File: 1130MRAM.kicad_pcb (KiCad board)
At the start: 4 copper layers, 228.6 x 63.5 mm, 159 parts, among them IC1 BSV52LT1G, IC10 BSV52LT1G, IC11 BSV52LT1G, IC12 BSV52LT1G, IC13 BSV52LT1G, IC14 BSV52LT1G, IC15 BSV52LT1G, IC16 BSV52LT1G, IC17 BSV52LT1G, IC18 BSV52LT1G, IC2 BSV52LT1G, IC3 BSV52LT1G, IC4 BSV52LT1G, IC5 BSV52LT1G, IC6 BSV52LT1G, IC7 BSV52LT1G, IC8 BSV52LT1G, IC9 BSV52LT1G, J1 Screw_Terminal_01x03, J1A09 SLTpad, J1A11 SLTpad, J2 Screw_Terminal_01x03, K1E09 SLTpad, K1E11 SLTpad, M1A09 SLTpad, M1A11 SLTpad, M1C09 SLTpad, M1D09 SLTpad, M1E09 SLTpad, M1E11 SLTpad, SW1 SLTpad, U1 MR0A16AYS35, U10 74LVC08A, U11 74LVC08A, U12 SN74LVC1G123DCUR, U13 SN74LVC1G123DCUR, U14 74HC00, U15 74HC86, U16 74HC86, U17 74HC86, U18 74HC86, U2 SN74LV240APWR, U3 SN74LV240APWR, U4 LDL1117, U5 SN74LVC1G123DCUR, U6 SN74LVC1G123DCUR, U7 74LVC08A, U8 74LVC08A, U9 74LVC08A

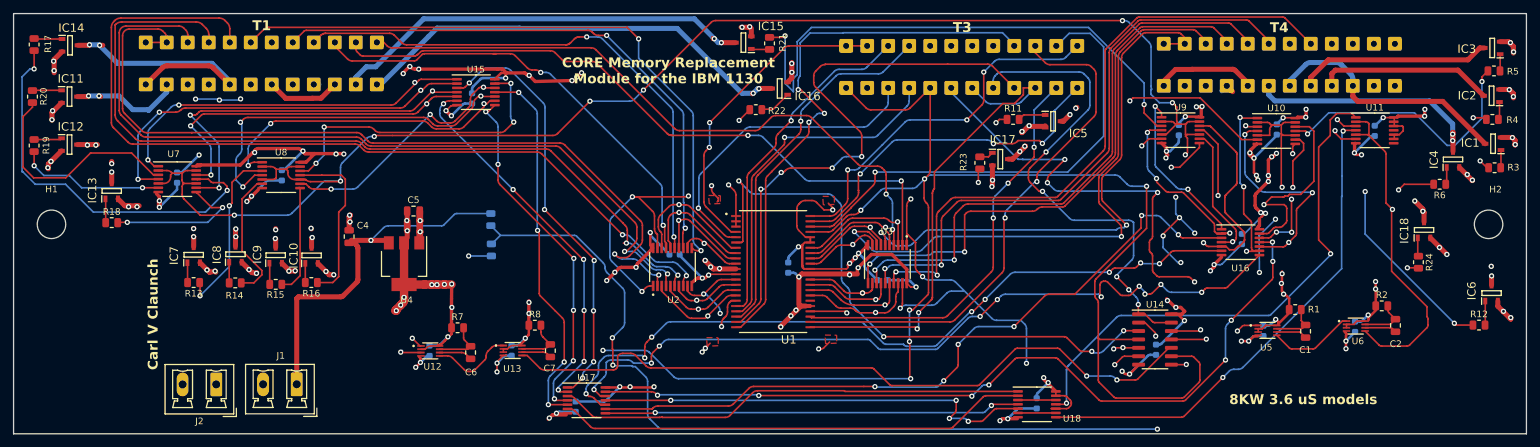
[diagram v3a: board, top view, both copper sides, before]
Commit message: New version leveraging FPGA
Changed board to be driven by an FPGA
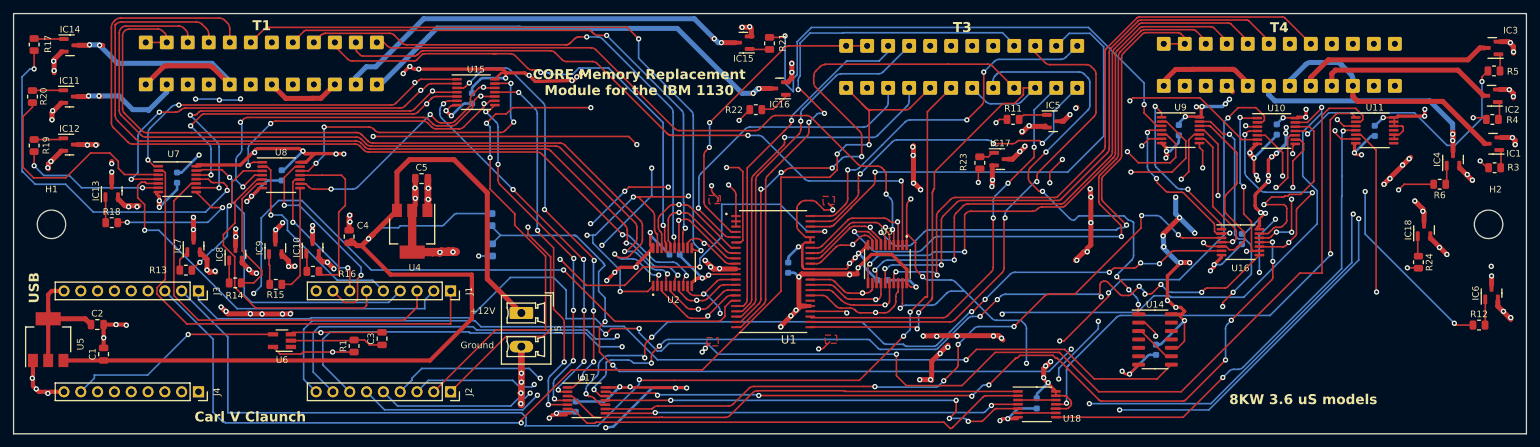
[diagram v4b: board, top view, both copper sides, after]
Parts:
- removed C14, C15, C22, C23: 0.1uF, Capacitor_SMD:C_0603_1608Metric
- removed C6: 680pF, Capacitor_SMD:C_0805_2012Metric
- removed C7: 47pF, Capacitor_SMD:C_0805_2012Metric
- removed R2, R7, R8: 1K, Resistor_SMD:R_0805_2012Metric
- removed U12, U13: SN74LVC1G123DCUR, 1130MRAM:sn74lvc1g123dcur
- added C3: 4.7u, Capacitor_SMD:C_0805_2012Metric, F.Cu at (88.7, 105.0)
- added J3: Conn_01x09_MountingPin, Connector_PinSocket_2.54mm:PinSocket_1x09_P2.54mm_Vertical, F.Cu at (61.0, 97.8)
- added J4: Conn_01x09_MountingPin, Connector_PinSocket_2.54mm:PinSocket_1x09_P2.54mm_Vertical, F.Cu at (61.0, 113.0)
- added J5: Screw_Terminal_01x03, Connector_Phoenix_MC_HighVoltage:PhoenixContact_MCV_1,5_2-G-5.08_1x02_P5.08mm_Vertical, F.Cu at (109.8, 101.1)
- C1: value 680pF -> 1uF
- C2: value 33pF -> 4.7uF
- IC1, IC10, IC11, IC12, IC13, IC14, IC15, IC16, IC17, IC18, IC2, IC3, IC4, IC5, IC6, IC7, IC8, IC9: footprint SamacSys_Parts:SOT95P237X111-3N -> Package_TO_SOT_SMD:SOT-23
- J1, J2: value Screw_Terminal_01x03 -> Conn_01x09_MountingPin; footprint Connector_Phoenix_MC_HighVoltage:PhoenixContact_MCV_1,5_2-G-5.08_1x02_P5.08mm_Vertical -> Connector_PinSocket_2.54mm:PinSocket_1x09_P2.54mm_Vertical
- R1: value 1K -> 330k
- U5: value SN74LVC1G123DCUR -> LDL1117; footprint 1130MRAM:sn74lvc1g123dcur -> Package_TO_SOT_SMD:SOT-223-3_TabPin2
- U6: value SN74LVC1G123DCUR -> 74LVC1G14; footprint 1130MRAM:sn74lvc1g123dcur -> Package_TO_SOT_SMD:SOT-23-5_HandSoldering
- moved C2 196.2 mm to (45.7, 102.9), turned to 0 degrees
- moved U5 184.2 mm to (38.2, 105.2), turned to 90 degrees
- moved C1 181.7 mm to (46.6, 107.3), turned to 90 degrees
- moved U6 162.3 mm to (73.6, 105.3), turned to 180 degrees
- moved R1 142.3 mm to (84.5, 106.1), turned to 90 degrees
- moved J2 35.4 mm to (99.1, 113.0), turned to -90 degrees
- moved J1 27.2 mm to (99.1, 97.8), turned to -90 degrees
- moved C5 5.05 mm to (94.7, 80.8)
- moved U4 5.05 mm to (93.2, 88.8)
- moved R13 2.21 mm to (59.0, 94.7)
- moved R16 1.72 mm to (78.2, 94.8)
- moved IC7 1.34 mm to (60.2, 91.0)
- moved IC10 1.22 mm to (78.2, 91.2)
- moved IC9 1.11 mm to (72.6, 91.3)
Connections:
- C1 pad 1: Net-(U5-REXT/CEXT) -> /+12V
- C1 pad 2: Net-(U5-CEXT) -> GND
- C2 pad 1: Net-(U6-REXT/CEXT) -> Net-(J3-Pin_9)
- C2 pad 2: Net-(U6-CEXT) -> GND
- J1 pad 1: /+12V -> Net-(J1-Pin_1)
- J1 pad 2: GND -> Net-(J1-Pin_2)
- J2 pad 1: GND -> Net-(J2-Pin_1)
- J2 pad 2: GND -> Net-(J2-Pin_2)
- R1 pad 2: Net-(U5-REXT/CEXT) -> Net-(C3-Pad1)
- SR1 pad 1: Net-(SR1-Pin_1) -> Net-(J3-Pin_2)
- U1 pad 17: Net-(U1-~{W}) -> Net-(J3-Pin_4)
- U1 pad 41: +SW -> Net-(J3-Pin_5)
- U1 pad 6: Net-(U1-~{E}) -> Net-(J3-Pin_6)
- U10 pad 10: Net-(U6-Q) -> Net-(J2-Pin_6)
- U10 pad 13: Net-(U6-Q) -> Net-(J2-Pin_7)
- U10 pad 2: Net-(U6-Q) -> Net-(J2-Pin_4)
- U10 pad 5: Net-(U6-Q) -> Net-(J2-Pin_5)
- U11 pad 2: Net-(U6-Q) -> Net-(J2-Pin_9)
- U11 pad 5: Net-(U6-Q) -> Net-(J2-Pin_8)
- U14 pad 10: Net-(U13-Q) -> +3.3V
- U14 pad 11: Net-(U5-~{A}) -> unconnected-(U14-Pad11)
- U14 pad 12: Net-(SR1-Pin_1) -> unconnected-(U14-Pad12)
- U14 pad 13: Net-(SU1-Pin_1) -> unconnected-(U14-Pad13)
- U14 pad 3: Net-(U1-~{E}) -> Net-(U14-Pad3)
- U14 pad 4: +SW -> unconnected-(U14-Pad4)
- U14 pad 5: +3.3V -> unconnected-(U14-Pad5)
- U14 pad 6: Net-(U2-~{1OE}) -> unconnected-(U14-Pad6)
- U14 pad 8: Net-(U1-~{W}) -> Net-(J3-Pin_1)
- U14 pad 9: +SW -> Net-(U14-Pad3)
- U2 pad 1: Net-(U2-~{1OE}) -> Net-(J3-Pin_8)
- U2 pad 19: Net-(U2-~{1OE}) -> Net-(J3-Pin_8)
- U3 pad 1: Net-(U2-~{1OE}) -> Net-(J3-Pin_8)
- U3 pad 19: Net-(U2-~{1OE}) -> Net-(J3-Pin_8)
- U5 pad 1: Net-(U5-~{A}) -> GND
- U5 pad 2: +3.3V -> Net-(J3-Pin_9)
- U5 pad 3: +3.3V -> /+12V
- U6 pad 1: Net-(U5-Q) -> (no net)
- U6 pad 2: +3.3V -> Net-(C3-Pad1)
- U6 pad 3: +3.3V -> GND
- U6 pad 4: GND -> Net-(J4-Pin_8)
- U6 pad 5: Net-(U6-Q) -> +3.3V
- U7 pad 10: Net-(U6-Q) -> Net-(J1-Pin_3)
- U7 pad 13: Net-(U6-Q) -> Net-(J1-Pin_4)
- U7 pad 2: Net-(U6-Q) -> Net-(J1-Pin_1)
- U7 pad 5: Net-(U6-Q) -> Net-(J1-Pin_2)
- U8 pad 10: Net-(U6-Q) -> Net-(J1-Pin_7)
- U8 pad 13: Net-(U6-Q) -> Net-(J1-Pin_8)
- U8 pad 2: Net-(U6-Q) -> Net-(J1-Pin_5)
- U8 pad 5: Net-(U6-Q) -> Net-(J1-Pin_6)
- U9 pad 10: Net-(U6-Q) -> Net-(J2-Pin_2)
- U9 pad 13: Net-(U6-Q) -> Net-(J2-Pin_3)
- U9 pad 2: Net-(U6-Q) -> Net-(J1-Pin_9)
- U9 pad 5: Net-(U6-Q) -> Net-(J2-Pin_1)
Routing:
- net Net-(U6-Q): track 336.4 -> 0.00 mm, vias 10 -> 0
- net Net-(J2-Pin_9): track 0.00 -> 217.3 mm, vias 0 -> 3
- net Net-(J3-Pin_8): track 0.00 -> 214.1 mm, vias 0 -> 8
- net Net-(J2-Pin_8): track 0.00 -> 203.6 mm, vias 0 -> 2
- net Net-(J2-Pin_7): track 0.00 -> 195.5 mm, vias 0 -> 3
- net Net-(J2-Pin_6): track 0.00 -> 193.7 mm, vias 0 -> 4
- net Net-(J2-Pin_5): track 0.00 -> 189.9 mm, vias 0 -> 4
- net Net-(J2-Pin_2): track 0.00 -> 179.8 mm, vias 0 -> 4
- net Net-(J3-Pin_2): track 0.00 -> 172.7 mm, vias 0 -> 3
- net Net-(J2-Pin_3): track 0.00 -> 165.4 mm, vias 0 -> 6
- net Net-(J3-Pin_1): track 0.00 -> 163.2 mm, vias 0 -> 1
- net Net-(J2-Pin_4): track 0.00 -> 162.5 mm, vias 0 -> 4
- net Net-(J1-Pin_9): track 0.00 -> 157.4 mm, vias 0 -> 3
- net Net-(J2-Pin_1): track 0.00 -> 147.3 mm, vias 0 -> 7
- net Net-(U2-~{1OE}): track 143.0 -> 0.00 mm, vias 8 -> 0
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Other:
- board text added: "+12V"
- board text added: "Ground"
- board text added: "USB"
